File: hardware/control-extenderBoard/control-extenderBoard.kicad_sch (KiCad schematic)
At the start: 148 parts, among them J1 12V + GND (TP), J10 SCL1 + GND (TP), J11 SDA1 + GND (TP), J12 3V3 + GND (TP), J13 12V + GND (TP), J14 SCL6 + GND (TP), J15 SDA6 + GND (TP), J17 24V IN, J18 GND, J22 SDA, SCL - ESP32, J23 I2C7 Reserve SCL/GND, J24 I2C6 Reserve SDA/GND, J25 I2C7 Reserve SDA/GND, J26 I2C6 Reserve SCL/GND, J27 CAT6-Shield, J28 CAT6-Shield, J29 Chassis, J3 Conn_01x02_Pin, J30 RX DIR, J31 TX, GND, J32 12V out, J33 5V out, J34 3V3 out, J35 Conn_01x02_Pin, J36 Conn_01x02_Pin, J37 Conn_01x02_Pin, J38 Conn_01x02_Pin, J39 Conn_01x02_Pin, J4 3V3 + GND (TP), J5 GND, J6 SCL7 Differential (TP), J7 SDA7 Differential (TP), J8 RS485, U1 MAX3485, U10 LM2576T-12, U2 PCA9600D, U3 TCA9548A_1-to-8_I2C_Multiplex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, U4 LM2576T-3.3, U5 PCA9600D, U6 PCA82C251, U7 PCA82C251, U8 PCA9600D, U9 LM2576T-5

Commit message: extenderBoard: Add ferrite-beads, Swap 12V TVS diodes
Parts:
- removed D11, D12, D8, D9: SMF12VTR, Diode_SMD:D_SOD-123F, symbol Diode:SMAJ150A
- added D11, D31, D8, D9: PESD12VL1BA, Diode_SMD:D_SOD-123F, symbol Device:D_TVS
- added D28: SMF12VTR, Diode_SMD:D_SOD-123F, symbol Diode:SMAJ150A
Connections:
- net GND: now also D11.1 (A1), D31.1 (A1), D8.1 (A1), D9.1 (A1)
- net SCL_Boost1: now also D9.2 (A2)
- net SCL_Boost2: now also D31.2 (A2)
- net SDA_Boost1: now also D11.2 (A2)
- net SDA_Boost2: now also D8.2 (A2)
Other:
- added sheet Remote-I2C-Sensor-Board1 (Remote-I2C-Sensor-Board.kicad_sch)
- note added: "SMF12VTR ideal (unidirectional) but too high C"

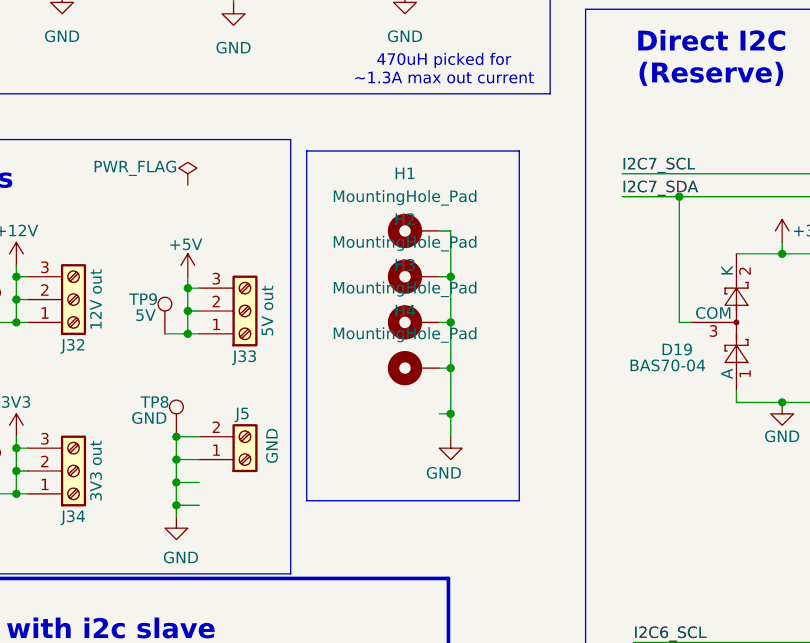
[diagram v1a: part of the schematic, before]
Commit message: extenderBoard: Optimize zones, routing, Fix errors - DRC pass
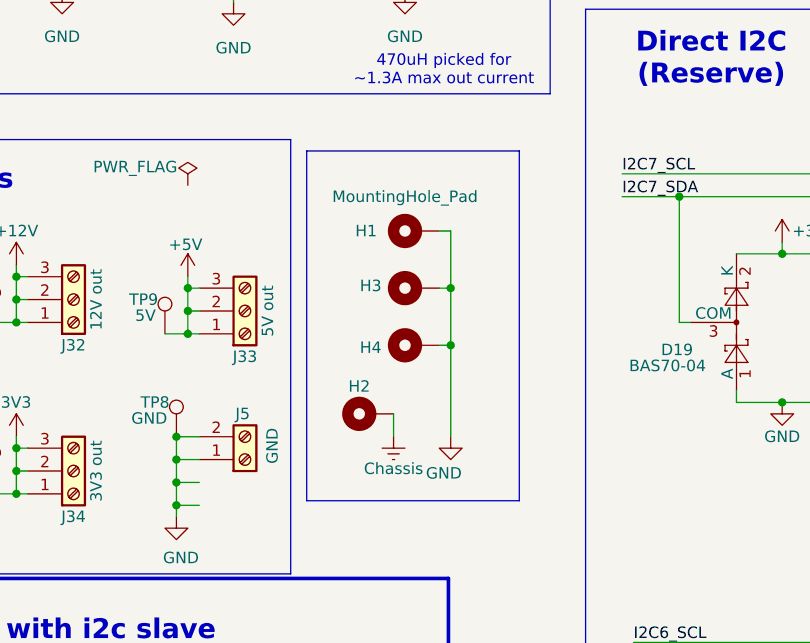
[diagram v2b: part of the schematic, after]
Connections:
- net Chassis: now also H2.1
- net GND: no longer H2.1
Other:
- moved on the sheet: H2, H3, H4
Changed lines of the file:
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@@
 	)
 	(junction
-		(at 93.98 215.9)
-		(diameter 0)
-		(color 0 0 0 0)
-	)
-	(junction
 		(at 342.9 40.64)
 		(diameter 0)
@@
 	)
 	(junction
-		(at 93.98 226.06)
-		(diameter 0)
-		(color 0 0 0 0)
-	)
-	(junction
 		(at 173.99 199.39)
 		(diameter 0)
@@
 	)
 	(junction
+		(at 93.98 218.44)
+		(diameter 0)
+		(color 0 0 0 0)
+	)
+	(junction
 		(at 64.77 212.09)
 		(diameter 0)
@@
 	)
 	(junction
-		(at 93.98 210.82)
-		(diameter 0)
-		(color 0 0 0 0)
-	)
-	(junction
 		(at 364.49 148.59)
 		(diameter 0)
@@
 	)
 	(junction
+		(at 93.98 212.09)
+		(diameter 0)
+		(color 0 0 0 0)
+	)
+	(junction
 		(at 45.72 232.41)
 		(diameter 0)
@@
 	)
 	(junction
-		(at 93.98 220.98)
-		(diameter 0)
-		(color 0 0 0 0)
-	)
-	(junction
 		(at 83.82 170.18)
 		(diameter 0)
@@
 	(wire
 		(pts
-			(xy 93.98 215.9) (xy 93.98 220.98)
-		)
-		(stroke
-			(width 0)
-			(type default)
-		)
-	)
-	(wire
-		(pts
 			(xy 163.83 254) (xy 167.64 254)
 		)
@@
 	(wire
 		(pts
-			(xy 92.71 226.06) (xy 93.98 226.06)
-		)
-		(stroke
-			(width 0)
-			(type default)
-		)
-	)
-	(wire
-		(pts
 			(xy 134.62 86.36) (xy 121.92 86.36)
 		)
@@
 	(wire
 		(pts
+			(xy 93.98 218.44) (xy 93.98 228.6)
+		)
+		(stroke
+			(width 0)
+			(type default)
+		)
+	)
+	(wire
+		(pts
 			(xy 360.68 227.33) (xy 363.22 227.33)
 		)
@@
 	(wire
 		(pts
-			(xy 93.98 205.74) (xy 93.98 210.82)
+			(xy 93.98 205.74) (xy 93.98 212.09)
 		)
 		(stroke
@@
 	(wire
 		(pts
-			(xy 92.71 220.98) (xy 93.98 220.98)
+			(xy 92.71 218.44) (xy 93.98 218.44)
 		)
 		(stroke
@@
 	(wire
 		(pts
-			(xy 92.71 215.9) (xy 93.98 215.9)
+			(xy 92.71 212.09) (xy 93.98 212.09)
 		)
 		(stroke
@@
 	(wire
 		(pts
+			(xy 93.98 212.09) (xy 93.98 218.44)
+		)
+		(stroke
+			(width 0)
+			(type default)
+		)
+	)
+	(wire
+		(pts
 			(xy 152.4 201.93) (xy 162.56 201.93)
 		)
@@
 	(wire
 		(pts
-			(xy 93.98 228.6) (xy 93.98 226.06)
-		)
-		(stroke
-			(width 0)
-			(type default)
-		)
-	)
-	(wire
-		(pts
 			(xy 59.69 34.29) (xy 66.04 34.29)
 		)
@@
 	(wire
 		(pts
-			(xy 92.71 210.82) (xy 93.98 210.82)
-		)
-		(stroke
-			(width 0)
-			(type default)
-		)
-	)
-	(wire
-		(pts
 			(xy 121.92 147.32) (xy 120.65 147.32)
 		)
@@
 	(wire
 		(pts
-			(xy 93.98 210.82) (xy 93.98 215.9)
-		)
-		(stroke
-			(width 0)
-			(type default)
-		)
-	)
-	(wire
-		(pts
 			(xy 158.75 187.96) (xy 158.75 189.23)
 		)
@@
 	(wire
 		(pts
+			(xy 87.63 228.6) (xy 87.63 226.06)
+		)
+		(stroke
+			(width 0)
+			(type default)
+		)
+	)
+	(wire
+		(pts
 			(xy 300.99 123.19) (xy 300.99 133.35)
 		)
@@
 	(wire
 		(pts
-			(xy 93.98 220.98) (xy 93.98 226.06)
-		)
-		(stroke
-			(width 0)
-			(type default)
-		)
-	)
-	(wire
-		(pts
 			(xy 358.14 218.44) (xy 358.14 217.17)
 		)
@@
 	)
 	(symbol
+		(lib_id "power:Earth")
+		(at 87.63 228.6 0)
+		(unit 1)
+		(exclude_from_sim no)
+		(in_bom yes)
+		(on_board yes)
+		(dnp no)
+		(property "Reference" "#PWR0136"
+			(at 87.63 234.95 0)
+			(effects
+				(font
+					(size 1.27 1.27)
+				)
+				(hide yes)
+			)
+		)
+		(property "Value" "Chassis"
+			(at 87.63 232.156 0)
+			(effects
+				(font
+					(size 1.27 1.27)
+				)
+			)
+		)
+		(property "Footprint" ""
+			(at 87.63 228.6 0)
+			(effects
+				(font
+					(size 1.27 1.27)
+				)
+				(hide yes)
+			)
+		)
+		(property "Datasheet" "~"
+			(at 87.63 228.6 0)
+			(effects
+				(font
+					(size 1.27 1.27)
+				)
+				(hide yes)
+			)
+		)
+		(property "Description" "Power symbol creates a global label with name \"Earth\""
+			(at 87.63 228.6 0)
+			(effects
+				(font
+					(size 1.27 1.27)
+				)
+				(hide yes)
+			)
+		)
+		(pin "1"
+		)
+		(instances
+			(project "control-extenderBoard"
+				(path "/e3fc34d4-dad6-4201-965b-dc5b1bdae059"
+					(reference "#PWR0136")
+					(unit 1)
+				)
+			)
+		)
+	)
+	(symbol
 		(lib_id "Interface_CAN_LIN:PCA82C251")
 		(at 341.63 121.92 0)
@@
 		(on_board yes)
 		(dnp no)
-		(fields_autoplaced yes)
 		(property "Reference" "H1"
-			(at 88.9 199.39 90)
+			(at 84.582 205.74 90)
 			(effects
 				(font
@@
 	(symbol
 		(lib_id "Mechanical:MountingHole_Pad")
-		(at 90.17 215.9 90)
+		(at 90.17 212.09 90)
 		(unit 1)
 		(exclude_from_sim no)
@@
 		(on_board yes)
 		(dnp no)
-		(fields_autoplaced yes)
 		(property "Reference" "H3"
-			(at 88.9 209.55 90)
+			(at 85.09 211.836 90)
 			(effects
 				(font
@@
 		)
 		(property "Value" "MountingHole_Pad"
-			(at 88.9 212.09 90)
+			(at 88.9 208.28 90)
 			(effects
 				(font
 					(size 1.27 1.27)
 				)
+				(hide yes)
 			)
 		)
 		(property "Footprint" "mountingHoles_libJonny:MountingHole_2.2mm_NPTH-with-pad_DRC-clearance-error"
-			(at 90.17 215.9 0)
+			(at 90.17 212.09 0)
 			(effects
 				(font
@@
 		)
 		(property "Datasheet" "~"
-			(at 90.17 215.9 0)
+			(at 90.17 212.09 0)
 			(effects
 				(font
@@
 		)
 		(property "Description" "Mounting Hole with connection"
-			(at 90.17 215.9 0)
+			(at 90.17 212.09 0)
 			(effects
 				(font
@@
 	(symbol
 		(lib_id "Mechanical:MountingHole_Pad")
-		(at 90.17 220.98 90)
+		(at 90.17 218.44 90)
 		(unit 1)
 		(exclude_from_sim no)
@@
 		(dnp no)
 		(property "Reference" "H4"
-			(at 88.9 214.63 90)
+			(at 85.09 218.694 90)
 			(effects
 				(font
@@
 		)
 		(property "Value" "MountingHole_Pad"
-			(at 88.9 217.17 90)
+			(at 88.9 214.63 90)
 			(effects
 				(font
 					(size 1.27 1.27)
 				)
+				(hide yes)
 			)
 		)
 		(property "Footprint" "mountingHoles_libJonny:MountingHole_2.2mm_NPTH-with-pad_DRC-clearance-error"
-			(at 90.17 220.98 0)
+			(at 90.17 218.44 0)
 			(effects
 				(font
@@
 		)
 		(property "Datasheet" "~"
-			(at 90.17 220.98 0)
+			(at 90.17 218.44 0)
 			(effects
 				(font
@@
 		)
 		(property "Description" "Mounting Hole with connection"
-			(at 90.17 220.98 0)
+			(at 90.17 218.44 0)
 			(effects
 				(font
@@
 	(symbol
 		(lib_id "Mechanical:MountingHole_Pad")
-		(at 90.17 210.82 90)
+		(at 85.09 226.06 90)
 		(unit 1)
 		(exclude_from_sim no)
@@
 		(on_board yes)
 		(dnp no)
-		(fields_autoplaced yes)
 		(property "Reference" "H2"
-			(at 88.9 204.47 90)
+			(at 83.82 223.012 90)
 			(effects
 				(font
@@
 		)
 		(property "Value" "MountingHole_Pad"
-			(at 88.9 207.01 90)
+			(at 83.82 222.25 90)
 			(effects
 				(font
 					(size 1.27 1.27)
 				)
+				(hide yes)
 			)
 		)
 		(property "Footprint" "mountingHoles_libJonny:MountingHole_2.2mm_NPTH-with-pad_DRC-clearance-error"
-			(at 90.17 210.82 0)
+			(at 85.09 226.06 0)
 			(effects
 				(font
@@
 		)
 		(property "Datasheet" "~"
-			(at 90.17 210.82 0)
+			(at 85.09 226.06 0)
 			(effects
 				(font
@@
 		)
 		(property "Description" "Mounting Hole with connection"
-			(at 90.17 210.82 0)
+			(at 85.09 226.06 0)
 			(effects
 				(font
